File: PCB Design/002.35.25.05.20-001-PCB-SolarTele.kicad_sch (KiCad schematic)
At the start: 33 parts, among them J1 Screw_Terminal_01x08, J2 Conn_01x01, J3 SMA, J4 SMA, J5 SMA, J6 SMA, J7 SMA, J8 SMA, U1 L7815, U2 L7805, U3 ADL5902ACPZ-R7, U4 LM358

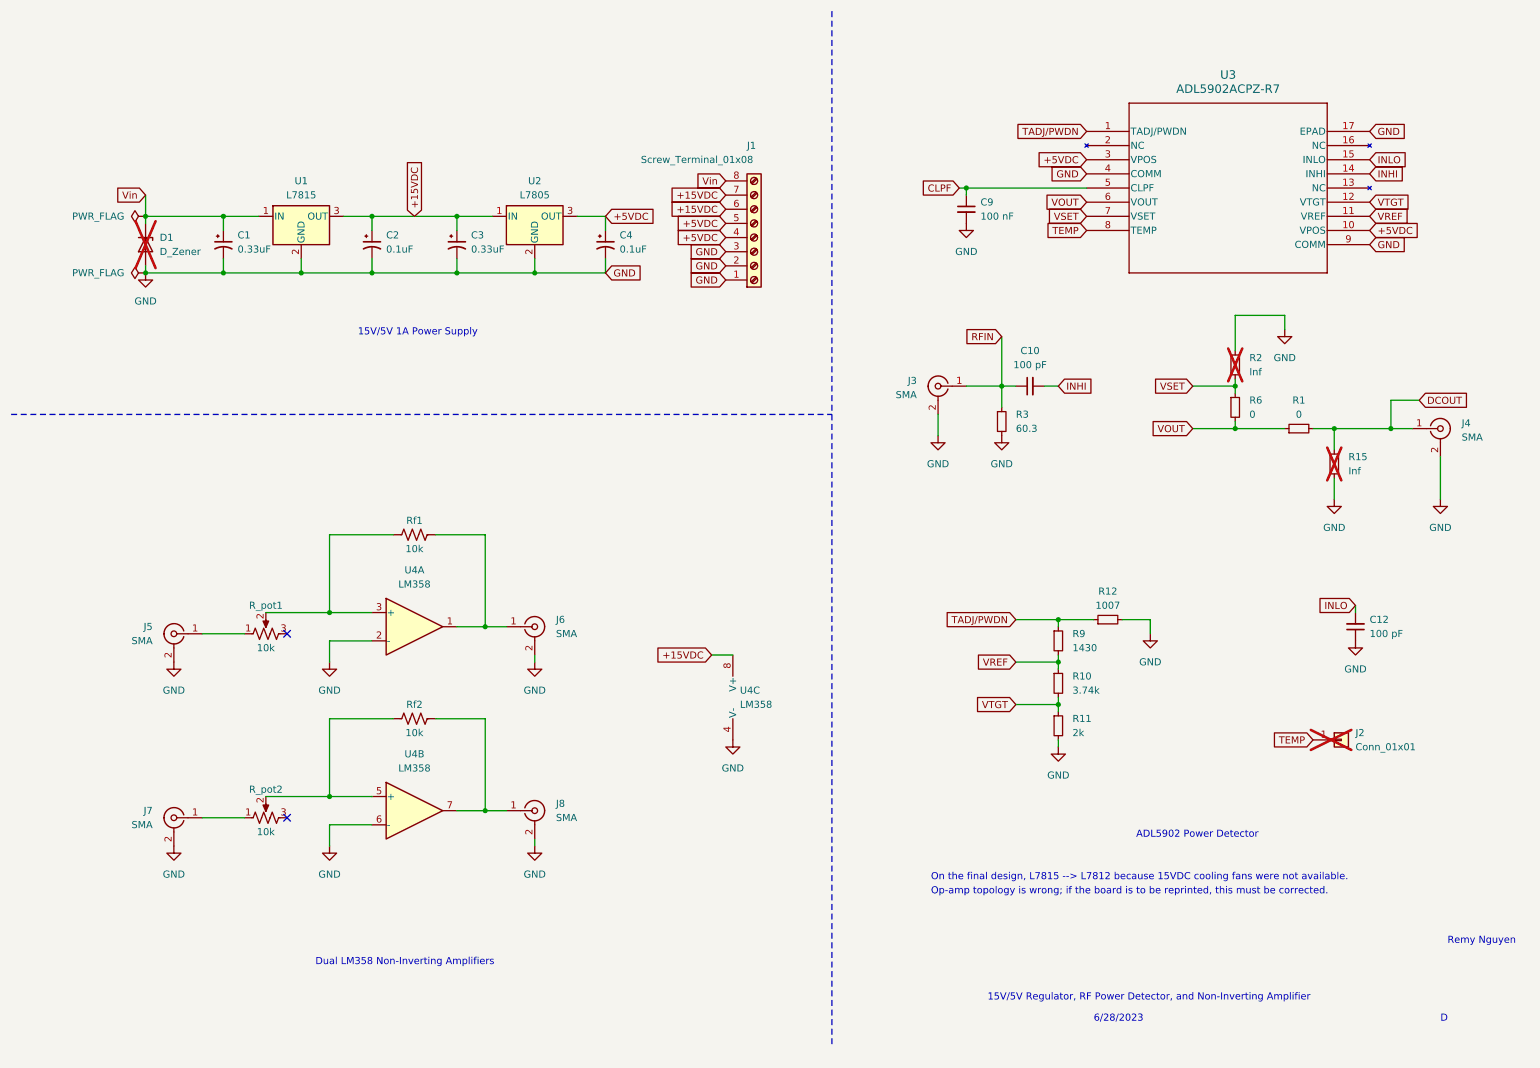
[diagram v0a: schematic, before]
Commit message: Fixed SMA pad thickness
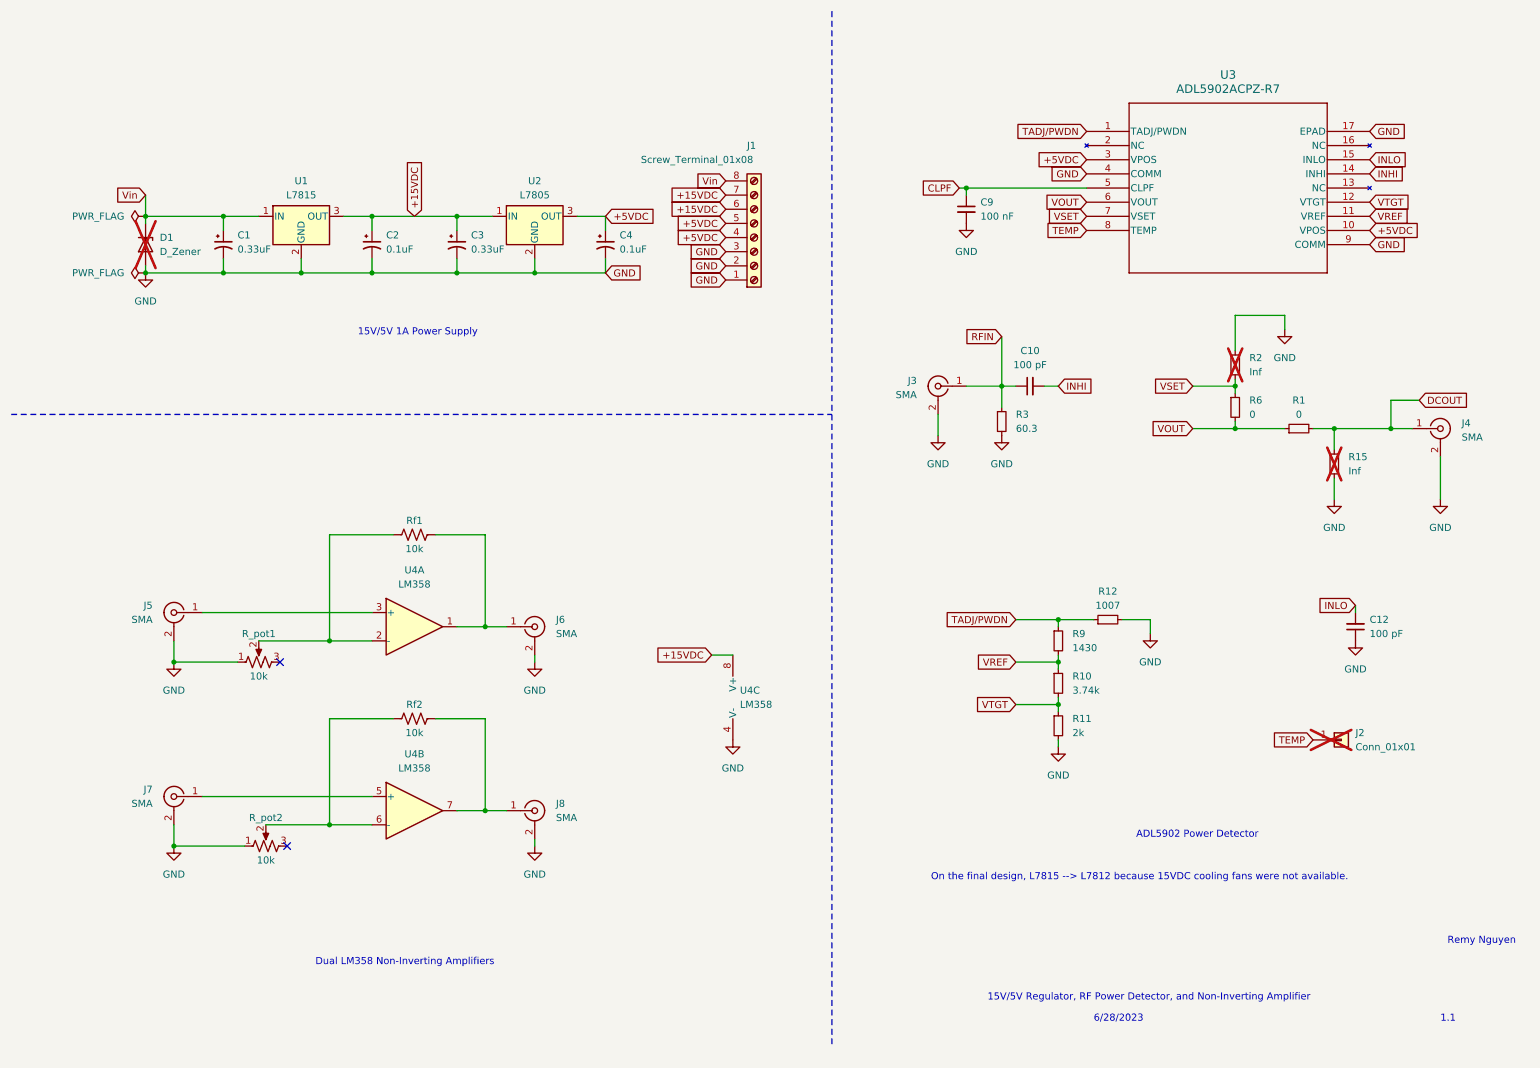
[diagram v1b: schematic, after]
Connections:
- net GND: now also R_pot1.1, R_pot2.1; no longer U4.2 (-), U4.6 (-)
- net at R_pot1.2, Rf1.1: now also U4.2 (-); no longer U4.3 (+)
- net at J7.1 (In): now also U4.5 (+); no longer R_pot2.1
- net at R_pot2.2, Rf2.1: now also U4.6 (-); no longer U4.5 (+)
- net at J5.1 (In): now also U4.3 (+); no longer R_pot1.1
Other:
- note added: "1.1"
- note removed: "D"
- note removed: "Op-amp topology is wrong; if the board is to be reprinted, this must be corrected."
- moved on the sheet: J5, J7, R_pot1, R_pot2

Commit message: PCB updated to Revision B, see changelog for details
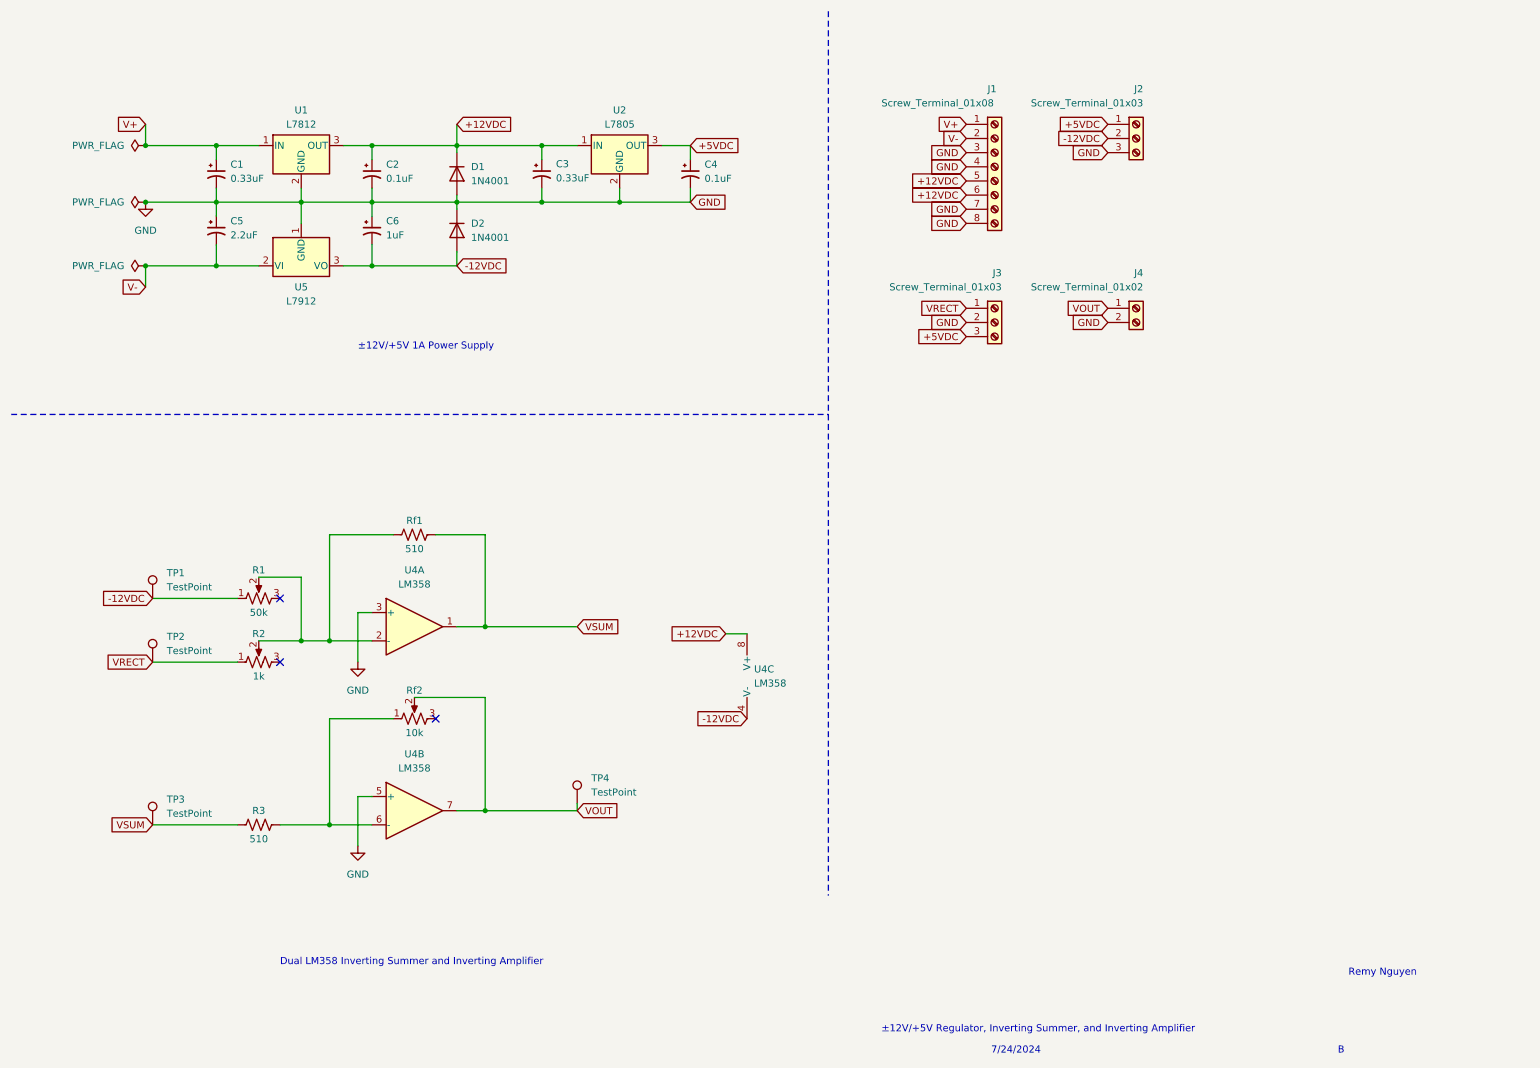
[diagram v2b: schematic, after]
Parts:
- removed C10, C12: 100 pF, Capacitor_SMD:C_1206_3216Metric, symbol Device:C_Small
- removed C9: 100 nF, Capacitor_SMD:C_0805_2012Metric, symbol Device:C_Small
- removed D1: D_Zener, Diode_SMD:D_1206_3216Metric, symbol Device:D_Zener
- removed J2: Conn_01x01, Connector_PinHeader_1.00mm:PinHeader_1x01_P1.00mm_Vertical, symbol Connector_Generic:Conn_01x01
- removed J3, J4, J5, J6, J7, J8: SMA, Connector_Coaxial:SMA_Molex_73251-1153_EdgeMount_Horizontal, symbol Connector:Conn_Coaxial
- removed R1, R6: 0, Resistor_SMD:R_0805_2012Metric, symbol Device:R_Small
- removed R10: 3.74k, Resistor_SMD:R_0805_2012Metric, symbol Device:R_Small
- removed R11: 2k, Resistor_SMD:R_0805_2012Metric, symbol Device:R_Small
- removed R12: 1007, Resistor_SMD:R_0805_2012Metric, symbol Device:R_Small
- removed R15, R2: Inf, Resistor_SMD:R_0805_2012Metric, symbol Device:R_Small
- removed R3: 60.3, Resistor_SMD:R_0805_2012Metric, symbol Device:R_Small
- removed R9: 1430, Resistor_SMD:R_0805_2012Metric, symbol Device:R_Small
- removed R_pot2: 10k, Potentiometer_THT:Potentiometer_Bourns_3006P_Horizontal, symbol Device:R_Potentiometer_US
- removed Rf2: 10k, Resistor_SMD:R_1206_3216Metric, symbol Device:R_US
- removed U1: L7815, Package_TO_SOT_THT:TO-220-3_Horizontal_TabDown, symbol Regulator_Linear:L7815
- removed U3: ADL5902ACPZ-R7, imports:CP_16_20_ADI, symbol AD5902ACPZ-R7:ADL5902ACPZ-R7
- added C5: 2.2uF, Capacitor_Tantalum_SMD:CP_EIA-3216-10_Kemet-I_Pad1.58x1.35mm_HandSolder, symbol Device:C_Polarized_Small_US
- added C6: 1uF, Capacitor_Tantalum_SMD:CP_EIA-3216-10_Kemet-I_Pad1.58x1.35mm_HandSolder, symbol Device:C_Polarized_Small_US
- added D1, D2: 1N4001, Diode_THT:D_DO-41_SOD81_P10.16mm_Horizontal, symbol Diode:1N4001
- added J2, J3: Screw_Terminal_01x03, TerminalBlock_Phoenix:TerminalBlock_Phoenix_MKDS-3-3-5.08_1x03_P5.08mm_Horizontal, symbol Connector:Screw_Terminal_01x03
- added J4: Screw_Terminal_01x02, TerminalBlock_Phoenix:TerminalBlock_Phoenix_MKDS-3-2-5.08_1x02_P5.08mm_Horizontal, symbol Connector:Screw_Terminal_01x02
- added R1: 50k, Potentiometer_THT:Potentiometer_Bourns_3386P_Vertical, symbol Device:R_Potentiometer_US
- added R3: 510, Resistor_THT:R_Axial_DIN0207_L6.3mm_D2.5mm_P7.62mm_Horizontal, symbol Device:R_US
- added Rf2: 10k, Potentiometer_THT:Potentiometer_Bourns_3386P_Vertical, symbol Device:R_Potentiometer_US
- added TP1, TP2, TP3, TP4: TestPoint, TestPoint:TestPoint_Loop_D2.54mm_Drill1.5mm_Beaded, symbol Connector:TestPoint
- added U1: L7812, Package_TO_SOT_SMD:TO-263-2, symbol Regulator_Linear:L7812
- added U5: L7912, Package_TO_SOT_SMD:TO-263-2, symbol Regulator_Linear:L7912
- C1, C2, C3, C4: footprint Capacitor_Tantalum_SMD:CP_EIA-2012-12_Kemet-R -> Capacitor_Tantalum_SMD:CP_EIA-3216-10_Kemet-I_Pad1.58x1.35mm_HandSolder
- R2: renamed from R_pot1; value 10k -> 1k; footprint Potentiometer_THT:Potentiometer_Bourns_3006P_Horizontal -> Potentiometer_THT:Potentiometer_Bourns_3386P_Vertical
- Rf1: value 10k -> 510; footprint Resistor_SMD:R_1206_3216Metric -> Resistor_THT:R_Axial_DIN0207_L6.3mm_D2.5mm_P7.62mm_Horizontal
- U2: footprint Package_TO_SOT_THT:TO-220-3_Horizontal_TabDown -> Package_TO_SOT_SMD:TO-263-2
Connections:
- net +5VDC: now also J2.1 (Pin_1), J3.3 (Pin_3); no longer J1.4 (Pin_4), J1.5 (Pin_5)
- net GND: now also J1.4 (Pin_4), J1.7 (Pin_7), J1.8 (Pin_8), U4.3 (+), U4.5 (+), C5.1, C6.1, D1.2 (A), D2.1 (K), J2.3 (Pin_3), J3.2 (Pin_2), J4.2 (Pin_2), U1.2 (GND), U5.1 (GND); no longer J1.1 (Pin_1), J1.2 (Pin_2), R2.1, U4.4 (V-)
- net VOUT: now also U4.7, J4.1 (Pin_1), Rf2.2, TP4.1
- net VSUM: now reaches Rf1.2, U4.1
- net VSUM: now also R3.1, TP3.1
- net at R2.2, Rf1.1, U4.2 (-): now also R1.2
- net at U4.6 (-): now also R3.2, Rf2.1
- net +15VDC renamed +12VDC
- net +12VDC: now also J1.5 (Pin_5), D1.1 (K), U1.3 (OUT); no longer J1.7 (Pin_7)
- net Vin renamed V+
- net V+: now also J1.1 (Pin_1), U1.1 (IN); no longer J1.8 (Pin_8)
- new net -12VDC: C6.2, D2.2 (A), J2.2 (Pin_2), R1.1, TP1.1, U4.4 (V-), U5.3 (VO)
- new net V-: C5.2, J1.2 (Pin_2), U5.2 (VI)
- new net VRECT: J3.1 (Pin_1), R2.1, TP2.1
- no-connect marks 2 -> 3
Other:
- note added: "7/24/2024"
- note added: "B"
- note added: "Dual LM358 Inverting Summer and Inverting Amplifier"
- note added: "±12V/+5V 1A Power Supply"
- note added: "±12V/+5V Regulator, Inverting Summer, and Inverting Amplifier"
- note removed: "1.1"
- note removed: "15V/5V 1A Power Supply"
- note removed: "15V/5V Regulator, RF Power Detector, and Non-Inverting Amplifier"
- note removed: "6/28/2023"
- note removed: "ADL5902 Power Detector"
- note removed: "Dual LM358 Non-Inverting Amplifiers"
- note removed: "On the final design, L7815 --> L7812 because 15VDC cooling fans were not available."
- moved on the sheet: C1, C2, C3, C4, J1, U2, U4C

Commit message: Housekeeping
- Updated schematic with higher value resistors to prevent backcurrent.
- Updated schematic with warning on low R2 value causing backcurrent.
- Removed KiCad/LaTeX auxiliary files and .gitignore'd them.
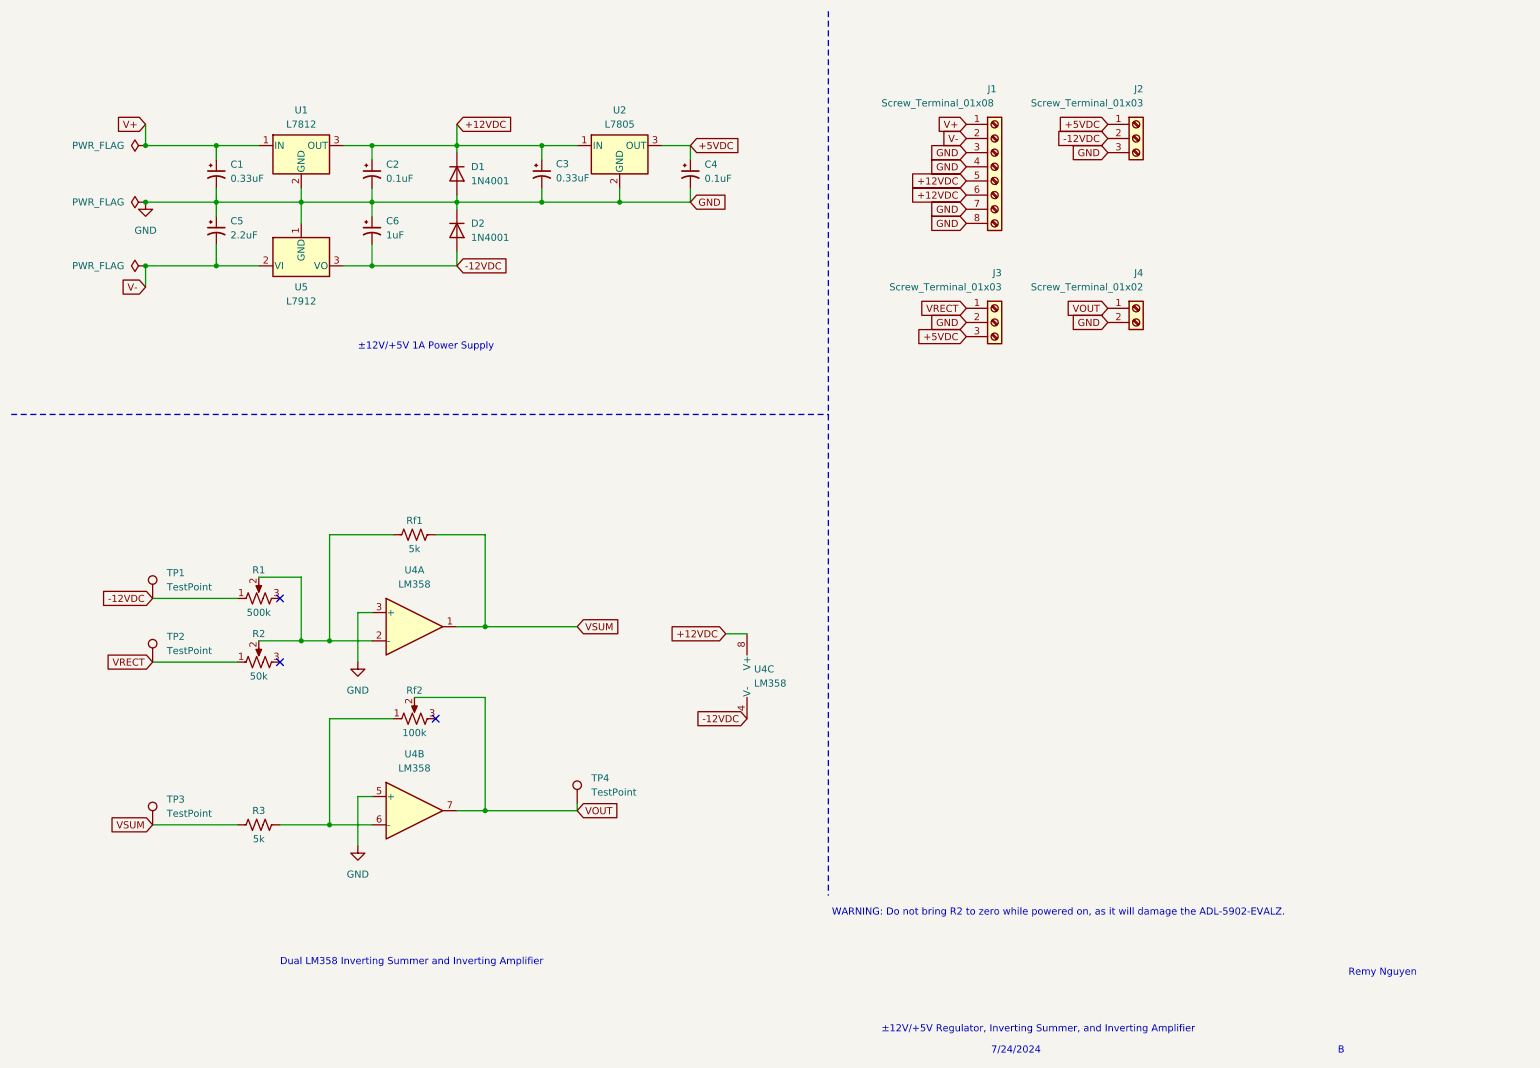
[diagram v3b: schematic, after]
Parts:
- R1: value 50k -> 500k
- R2: value 1k -> 50k
- R3, Rf1: value 510 -> 5k
- Rf2: value 10k -> 100k
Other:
- note added: "WARNING: Do not bring R2 to zero while powered on, as it will damage the ADL-5902-EVALZ."
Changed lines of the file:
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@@
+    (effects (font (size 1.27 1.27)) (justify left bottom))
+  )
+  (text "WARNING: Do not bring R2 to zero while powered on, as it will damage the ADL-5902-EVALZ."
+    (at 160.02 175.26 0)
     (effects (font (size 1.27 1.27)) (justify left bottom))
   )
@@
       (effects (font (size 1.27 1.27)))
     )
-    (property "Value" "510" (at 57.15 161.29 90)
+    (property "Value" "5k" (at 57.15 161.29 90)
       (effects (font (size 1.27 1.27)))
     )
@@
       (effects (font (size 1.27 1.27)))
     )
-    (property "Value" "510" (at 85.09 109.22 90)
+    (property "Value" "5k" (at 85.09 109.22 90)
       (effects (font (size 1.27 1.27)))
     )
@@
       (effects (font (size 1.27 1.27)))
     )
-    (property "Value" "50k" (at 57.15 120.65 90)
+    (property "Value" "500k" (at 57.15 120.65 90)
       (effects (font (size 1.27 1.27)))
     )
@@
       (effects (font (size 1.27 1.27)))
     )
-    (property "Value" "1k" (at 57.15 132.08 90)
+    (property "Value" "50k" (at 57.15 132.08 90)
       (effects (font (size 1.27 1.27)))
     )
@@
       (effects (font (size 1.27 1.27)))
     )
-    (property "Value" "10k" (at 85.09 142.24 90)
-      (effects (font (size 1.27 1.27)))
-    )
+    (property "Value" "100k" (at 85.09 142.24 90)
+      (effects (font (size 1.27 1.27)))
+    )
